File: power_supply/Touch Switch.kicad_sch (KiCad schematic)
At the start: 51 parts, among them J1 Conn_01x01_Pin, J2 Conn_02x04_Counter_Clockwise, J3 Conn_01x01_Pin, J4 Conn_01x01_Pin, J5 Conn_01x01_Pin, J6 Conn_01x01_Pin, J7 Conn_01x01_Pin, J8 Conn_01x01_Pin, K1 Relay_SPST-NO, K2 Relay_SPST-NO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

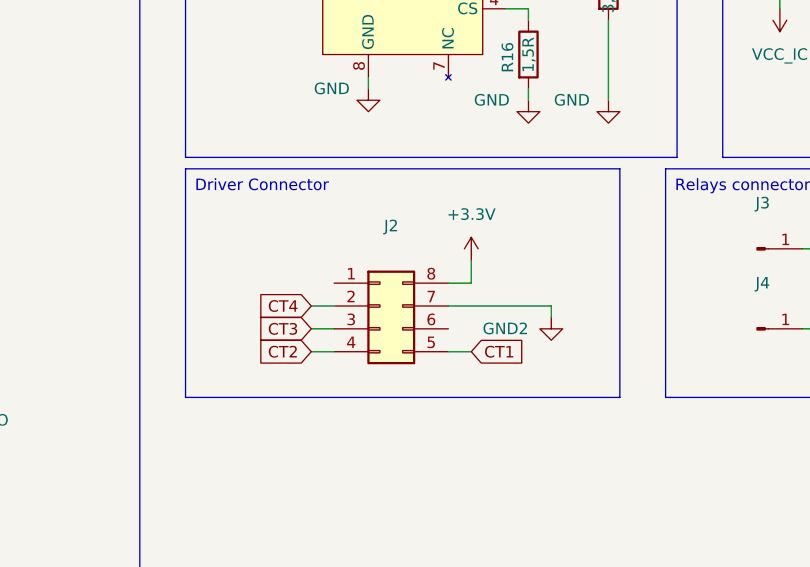
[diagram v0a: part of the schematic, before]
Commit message: PCB (control_card) : V3 finished, perfect dimension
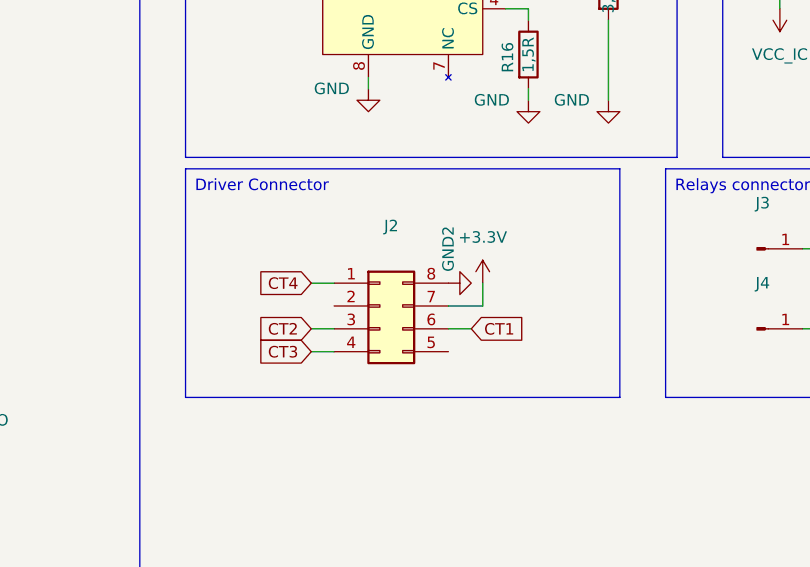
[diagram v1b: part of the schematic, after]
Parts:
- J2: footprint Connector_PinSocket_2.54mm:PinSocket_2x04_P2.54mm_Vertical -> Footprint_Rang_Dong:Female connector
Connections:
- net +3.3V: now also J2.7 (Pin_7); no longer J2.8 (Pin_8)
- net CT1: now also J2.6 (Pin_6); no longer J2.5 (Pin_5)
- net CT2: now also J2.3 (Pin_3); no longer J2.4 (Pin_4)
- net CT3: now also J2.4 (Pin_4); no longer J2.3 (Pin_3)
- net CT4: now also J2.1 (Pin_1); no longer J2.2 (Pin_2)
- net GND2: now also J2.8 (Pin_8); no longer J2.7 (Pin_7)
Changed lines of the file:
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@@
 	(wire
 		(pts
-			(xy 234.95 95.25) (xy 234.95 97.79)
+			(xy 201.93 128.27) (xy 201.93 130.81)
 		)
 		(stroke
@@
 	(wire
 		(pts
-			(xy 46.99 162.56) (xy 46.99 160.02)
+			(xy 234.95 95.25) (xy 234.95 97.79)
 		)
 		(stroke
@@
 	(wire
 		(pts
-			(xy 129.54 29.21) (xy 129.54 31.75)
+			(xy 46.99 162.56) (xy 46.99 160.02)
 		)
 		(stroke
@@
 	(wire
 		(pts
-			(xy 200.66 125.73) (xy 200.66 128.27)
+			(xy 129.54 29.21) (xy 129.54 31.75)
 		)
 		(stroke
@@
 	(wire
 		(pts
+			(xy 182.88 135.89) (xy 185.42 135.89)
+		)
+		(stroke
+			(width 0)
+			(type default)
+		)
+	)
+	(wire
+		(pts
 			(xy 63.5 77.47) (xy 63.5 80.01)
 		)
@@
 	(wire
 		(pts
-			(xy 182.88 135.89) (xy 185.42 135.89)
-		)
-		(stroke
-			(width 0)
-			(type default)
-		)
-	)
-	(wire
-		(pts
-			(xy 182.88 133.35) (xy 185.42 133.35)
-		)
-		(stroke
-			(width 0)
-			(type default)
-		)
-	)
-	(wire
-		(pts
 			(xy 113.03 165.1) (xy 113.03 172.72)
 		)
@@
 	(wire
 		(pts
+			(xy 198.12 130.81) (xy 201.93 130.81)
+		)
+		(stroke
+			(width 0)
+			(type default)
+		)
+	)
+	(wire
+		(pts
 			(xy 218.44 39.37) (xy 226.06 39.37)
 		)
@@
 	(wire
 		(pts
-			(xy 45.72 38.1) (xy 45.72 40.64)
+			(xy 182.88 128.27) (xy 185.42 128.27)
 		)
 		(stroke
@@
 	(wire
 		(pts
-			(xy 179.07 95.25) (xy 181.61 95.25)
+			(xy 45.72 38.1) (xy 45.72 40.64)
 		)
 		(stroke
@@
 	(wire
 		(pts
-			(xy 209.55 130.81) (xy 209.55 132.08)
+			(xy 179.07 95.25) (xy 181.61 95.25)
 		)
 		(stroke
@@
 	(wire
 		(pts
-			(xy 198.12 135.89) (xy 200.66 135.89)
+			(xy 111.76 76.2) (xy 116.84 76.2)
 		)
 		(stroke
@@
 	(wire
 		(pts
-			(xy 111.76 76.2) (xy 116.84 76.2)
+			(xy 257.81 39.37) (xy 265.43 39.37)
 		)
 		(stroke
@@
 	(wire
 		(pts
-			(xy 257.81 39.37) (xy 265.43 39.37)
+			(xy 57.15 29.21) (xy 68.58 29.21)
 		)
 		(stroke
@@
 	(wire
 		(pts
-			(xy 57.15 29.21) (xy 68.58 29.21)
+			(xy 132.08 132.08) (xy 133.35 132.08)
 		)
 		(stroke
@@
 	(wire
 		(pts
-			(xy 132.08 132.08) (xy 133.35 132.08)
+			(xy 182.88 133.35) (xy 185.42 133.35)
 		)
 		(stroke
@@
 	(wire
 		(pts
-			(xy 198.12 130.81) (xy 209.55 130.81)
-		)
-		(stroke
-			(width 0)
-			(type default)
-		)
-	)
-	(wire
-		(pts
 			(xy 233.68 48.26) (xy 250.19 48.26)
 		)
@@
 	(wire
 		(pts
-			(xy 182.88 130.81) (xy 185.42 130.81)
-		)
-		(stroke
-			(width 0)
-			(type default)
-		)
-	)
-	(wire
-		(pts
 			(xy 207.01 97.79) (xy 207.01 99.06)
 		)
@@
 	(wire
 		(pts
-			(xy 200.66 128.27) (xy 198.12 128.27)
-		)
-		(stroke
-			(width 0)
-			(type default)
-		)
-	)
-	(wire
-		(pts
 			(xy 181.61 53.34) (xy 181.61 54.61)
 		)
@@
 	(wire
 		(pts
+			(xy 198.12 133.35) (xy 200.66 133.35)
+		)
+		(stroke
+			(width 0)
+			(type default)
+		)
+	)
+	(wire
+		(pts
 			(xy 41.91 160.02) (xy 46.99 160.02)
 		)
@@
 	(global_label "CT2"
 		(shape input)
-		(at 182.88 135.89 180)
+		(at 182.88 133.35 180)
 		(fields_autoplaced yes)
 		(effects
@@
 		)
 		(property "Intersheetrefs" "${INTERSHEET_REFS}"
-			(at 176.4477 135.89 0)
+			(at 176.4477 133.35 0)
 			(effects
 				(font
@@
 	(global_label "CT1"
 		(shape input)
-		(at 200.66 135.89 0)
+		(at 200.66 133.35 0)
 		(fields_autoplaced yes)
 		(effects
@@
 		)
 		(property "Intersheetrefs" "${INTERSHEET_REFS}"
-			(at 207.0923 135.89 0)
+			(at 207.0923 133.35 0)
 			(effects
 				(font
@@
 	(global_label "CT4"
 		(shape input)
-		(at 182.88 130.81 180)
+		(at 182.88 128.27 180)
 		(fields_autoplaced yes)
 		(effects
@@
 		)
 		(property "Intersheetrefs" "${INTERSHEET_REFS}"
-			(at 176.4477 130.81 0)
+			(at 176.4477 128.27 0)
 			(effects
 				(font
@@
 	(global_label "CT3"
 		(shape input)
-		(at 182.88 133.35 180)
+		(at 182.88 135.89 180)
 		(fields_autoplaced yes)
 		(effects
@@
 		)
 		(property "Intersheetrefs" "${INTERSHEET_REFS}"
-			(at 176.4477 133.35 0)
+			(at 176.4477 135.89 0)
 			(effects
 				(font
@@
 			)
 		)
-		(property "Footprint" "Connector_PinSocket_2.54mm:PinSocket_2x04_P2.54mm_Vertical"
+		(property "Footprint" "Footprint_Rang_Dong:Female connector"
 			(at 190.5 130.81 0)
 			(effects
@@
 	(symbol
 		(lib_id "power:+3.3V")
-		(at 200.66 125.73 0)
+		(at 201.93 128.27 0)
 		(unit 1)
 		(exclude_from_sim no)
@@
 		(fields_autoplaced yes)
 		(property "Reference" "#PWR032"
-			(at 200.66 129.54 0)
+			(at 201.93 132.08 0)
 			(effects
 				(font
@@
 		)
 		(property "Value" "+3.3V"
-			(at 200.66 120.65 0)
+			(at 201.93 123.19 0)
 			(effects
 				(font
@@
 		)
 		(property "Footprint" ""
-			(at 200.66 125.73 0)
+			(at 201.93 128.27 0)
 			(effects
 				(font
@@
 		)
 		(property "Datasheet" ""
-			(at 200.66 125.73 0)
+			(at 201.93 128.27 0)
 			(effects
 				(font
@@
 		)
 		(property "Description" "Power symbol creates a global label with name \"+3.3V\""
-			(at 200.66 125.73 0)
+			(at 201.93 128.27 0)
 			(effects
 				(font
@@
 	(symbol
 		(lib_id "power:GND2")
-		(at 209.55 132.08 0)
+		(at 198.12 128.27 90)
 		(unit 1)
 		(exclude_from_sim no)
@@
 		(dnp no)
 		(property "Reference" "#PWR033"
-			(at 209.55 138.43 0)
+			(at 204.47 128.27 0)
 			(effects
 				(font
@@
 		)
 		(property "Value" "GND2"
-			(at 204.47 133.35 0)
+			(at 198.12 124.46 0)
 			(effects
 				(font
@@
 		)
 		(property "Footprint" ""
-			(at 209.55 132.08 0)
+			(at 198.12 128.27 0)
 			(effects
 				(font
@@
 		)
 		(property "Datasheet" ""
-			(at 209.55 132.08 0)
+			(at 198.12 128.27 0)
 			(effects
 				(font
@@
 		)
 		(property "Description" "Power symbol creates a global label with name \"GND2\" , ground"
-			(at 209.55 132.08 0)
+			(at 198.12 128.27 0)
 			(effects
 				(font
